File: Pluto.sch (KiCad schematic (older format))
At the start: 1 part, among them U1 OUTLINE

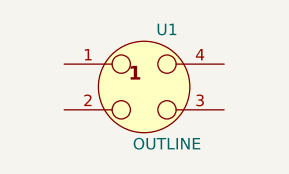
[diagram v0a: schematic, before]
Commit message: Finish schematic
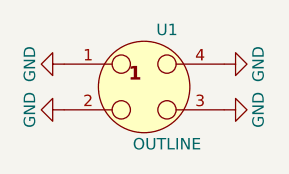
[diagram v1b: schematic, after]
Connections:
- net GND: now reaches U1.1
- net GND: now also U1.2, U1.3, U1.4
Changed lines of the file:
@@
 LIBS:contrib
 LIBS:valves
+LIBS:Pluto-cache
 EELAYER 25 0
 EELAYER END
@@
 	1    0    0    -1
 $EndComp
+$Comp
+L GND #PWR?
+U 1 1 59EE3745
+P 2675 2000
+F 0 "#PWR?" H 2675 1750 50  0001 C CNN
+F 1 "GND" H 2675 1850 50  0000 C CNN
+F 2 "" H 2675 2000 50  0001 C CNN
+F 3 "" H 2675 2000 50  0001 C CNN
+	1    2675 2000
+	0    1    1    0
+$EndComp
+$Comp
+L GND #PWR?
+U 1 1 59EE375B
+P 2675 2200
+F 0 "#PWR?" H 2675 1950 50  0001 C CNN
+F 1 "GND" H 2675 2050 50  0000 C CNN
+F 2 "" H 2675 2200 50  0001 C CNN
+F 3 "" H 2675 2200 50  0001 C CNN
+	1    2675 2200
+	0    1    1    0
+$EndComp
+$Comp
+L GND #PWR?
+U 1 1 59EE3771
+P 3375 2000
+F 0 "#PWR?" H 3375 1750 50  0001 C CNN
+F 1 "GND" H 3375 1850 50  0000 C CNN
+F 2 "" H 3375 2000 50  0001 C CNN
+F 3 "" H 3375 2000 50  0001 C CNN
+	1    3375 2000
+	0    -1   -1   0
+$EndComp
+$Comp
+L GND #PWR?
+U 1 1 59EE3787
+P 3375 2200
+F 0 "#PWR?" H 3375 1950 50  0001 C CNN
+F 1 "GND" H 3375 2050 50  0000 C CNN
+F 2 "" H 3375 2200 50  0001 C CNN
+F 3 "" H 3375 2200 50  0001 C CNN
+	1    3375 2200
+	0    -1   -1   0
+$EndComp
 $EndSCHEMATC
